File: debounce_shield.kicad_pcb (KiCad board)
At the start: 2 copper layers, 65 x 56 mm, 75 parts, among them IC1 LTV-814, IC2 LTV-814, IC3 LTV-814, IC4 LTV-814, IC5 LTV-814, IC6 LTV-814, IC7 MAX16914AUB+, J1 Conn_01x06, J2 RPi_GPIO, J3 Conn_01x06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

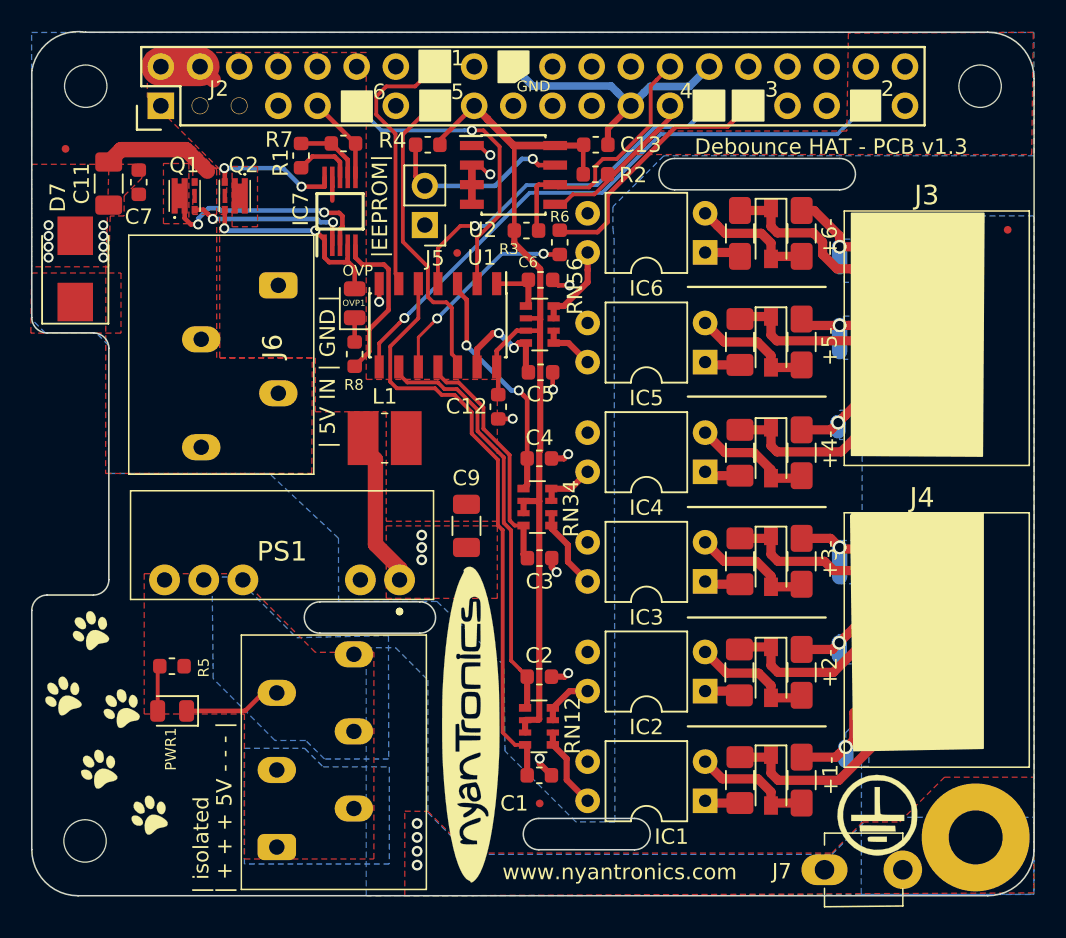
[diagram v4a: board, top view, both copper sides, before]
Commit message: Add additional filtering and protection to DC-DC circuit.
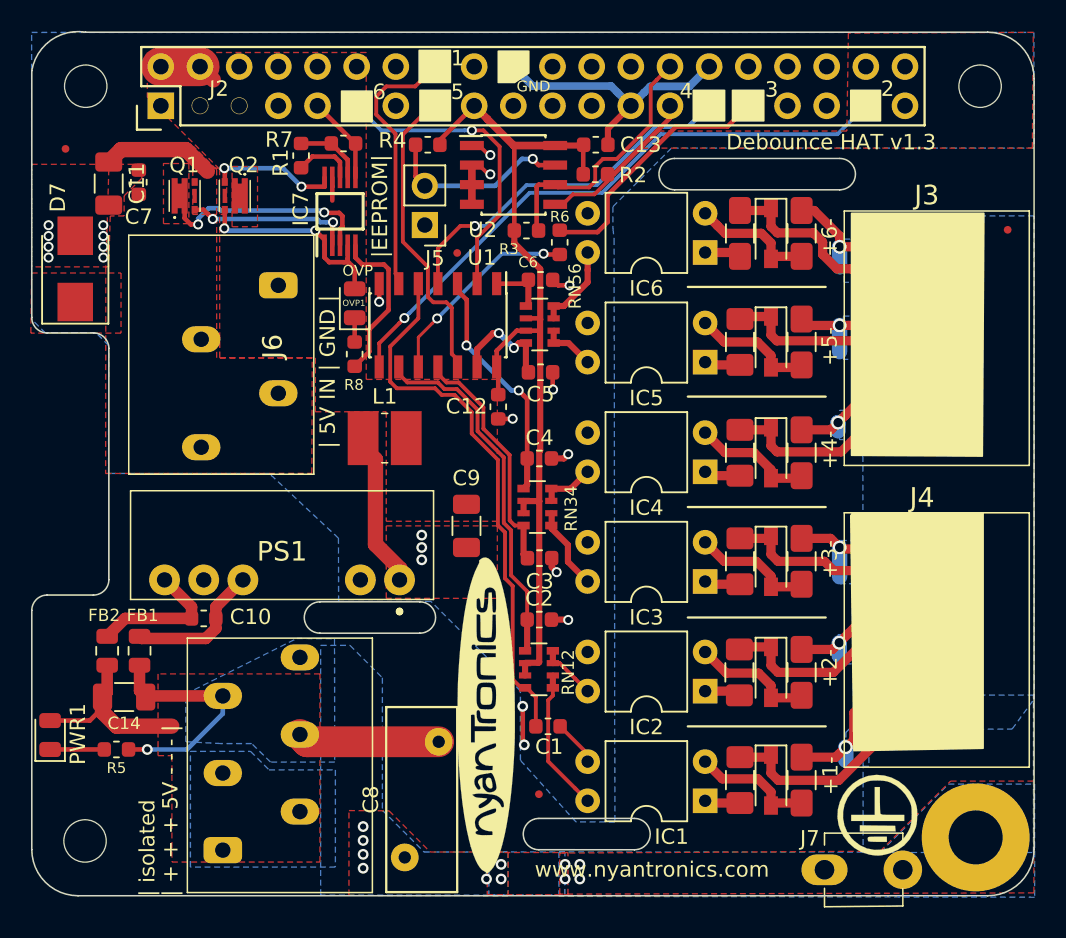
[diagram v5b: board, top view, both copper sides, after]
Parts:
- added C10: 100nF/50V, Capacitor_SMD:C_0603_1608Metric, F.Cu at (108.7, 110.6)
- added C14: 10uF/25V, Capacitor_SMD:C_1206_3216Metric, F.Cu at (103.5, 115.7)
- added C8: 220pF/440VAC, Varistor:RV_Disc_D12mm_W4.6mm_P7.5mm, F.Cu at (123.9, 118.6)
- added FB1: FB, Inductor_SMD:L_0805_2012Metric, F.Cu at (104.5, 112.7)
- added FB2: FB, Inductor_SMD:L_0805_2012Metric, F.Cu at (102.4, 112.7)
- C1, C12, C13, C2, C3, C4, C5, C6, C7: value 100 nF -> 100nF
- C11: value 10uF -> 10uF/35V
- C9: value 10uF -> 10uF/25V
- G***: moved to B.Cu
- PS1: value RKZE-0505S -> RKZE-0505S/H
- moved G*** 29.8 mm to (119.7, 92.4), turned to 180 degrees
- moved PWR1 8.07 mm to (98.7, 118.2), turned to 90 degrees
- moved R5 6.49 mm to (103.0, 119.1), turned to 0 degrees
- moved C2 3.70 mm to (130.4, 110.7)
- moved RN12 3.70 mm to (130.4, 113.9)
- moved J1 3.51 mm to (114.9, 113.1)
- moved C1 3.23 mm to (131.0, 117.6)
- moved G*** 1.17 mm to (126.9, 116.9)
- moved REF** 0.60 mm to (130.4, 122.0)
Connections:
- J1 pad 1: Net-(J1-Pad1) -> Net-(C14-Pad1)
- J1 pad 2: Net-(J1-Pad1) -> Net-(C14-Pad1)
- J1 pad 3: Net-(J1-Pad1) -> Net-(C14-Pad1)
- J1 pad 4: Net-(J1-Pad4) -> Net-(C14-Pad2)
- J1 pad 5: Net-(J1-Pad4) -> Net-(C14-Pad2)
- J1 pad 6: Net-(J1-Pad4) -> Net-(C14-Pad2)
- PS1 pad 5: Net-(J1-Pad4) -> Net-(C10-Pad2)
- PS1 pad 7: Net-(J1-Pad1) -> Net-(C10-Pad1)
- PWR1 pad 1: Net-(J1-Pad4) -> Net-(PWR1-Pad1)
- PWR1 pad 2: Net-(PWR1-Pad2) -> Net-(C14-Pad1)
- R5 pad 1: Net-(J1-Pad1) -> Net-(PWR1-Pad1)
- R5 pad 2: Net-(PWR1-Pad2) -> Net-(C14-Pad2)
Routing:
- net Net-(C14-Pad2): track 0.00 -> 25.3 mm, vias 0 -> 1
- net Net-(C14-Pad1): track 0.00 -> 11.7 mm
- net Net-(C10-Pad1): track 0.00 -> 9.29 mm
- net Net-(C10-Pad2): track 0.00 -> 9.20 mm
- net Net-(J1-Pad4): track 6.48 -> 0.00 mm
- net GND: track 40.1 -> 44.2 mm, vias 21 -> 22
- net Net-(IC1-Pad4): track 5.36 -> 9.31 mm
- net Net-(C2-Pad2): track 27.2 -> 23.5 mm
- net +3.3V: track 62.9 -> 59.2 mm
- net Net-(PWR1-Pad1): track 0.00 -> 3.51 mm
- net Net-(C1-Pad2): track 38.6 -> 35.5 mm
- net Net-(PWR1-Pad2): track 2.96 -> 0.00 mm
- net PE: vias 4 -> 12
- added copper zone on B.Cu, net Net-(C14-Pad1)
- added copper zone on F.Cu, net Net-(C14-Pad1)
- added copper zone on B.Cu, net Net-(C14-Pad2)
- removed copper zone on B.Cu, net Net-(J1-Pad1)
- removed copper zone on F.Cu, net Net-(J1-Pad1)
- removed copper zone on B.Cu, net Net-(J1-Pad4)
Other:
- board text added: "Debounce HAT v1.3"
- board text removed: "Debounce HAT - PCB v1.3"
